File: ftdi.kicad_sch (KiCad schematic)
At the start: 24 parts, among them U1 FT2232H-56Q, U11 93LC56CT-IMC, Y4 ABM8G-12M-18-D2Y-T

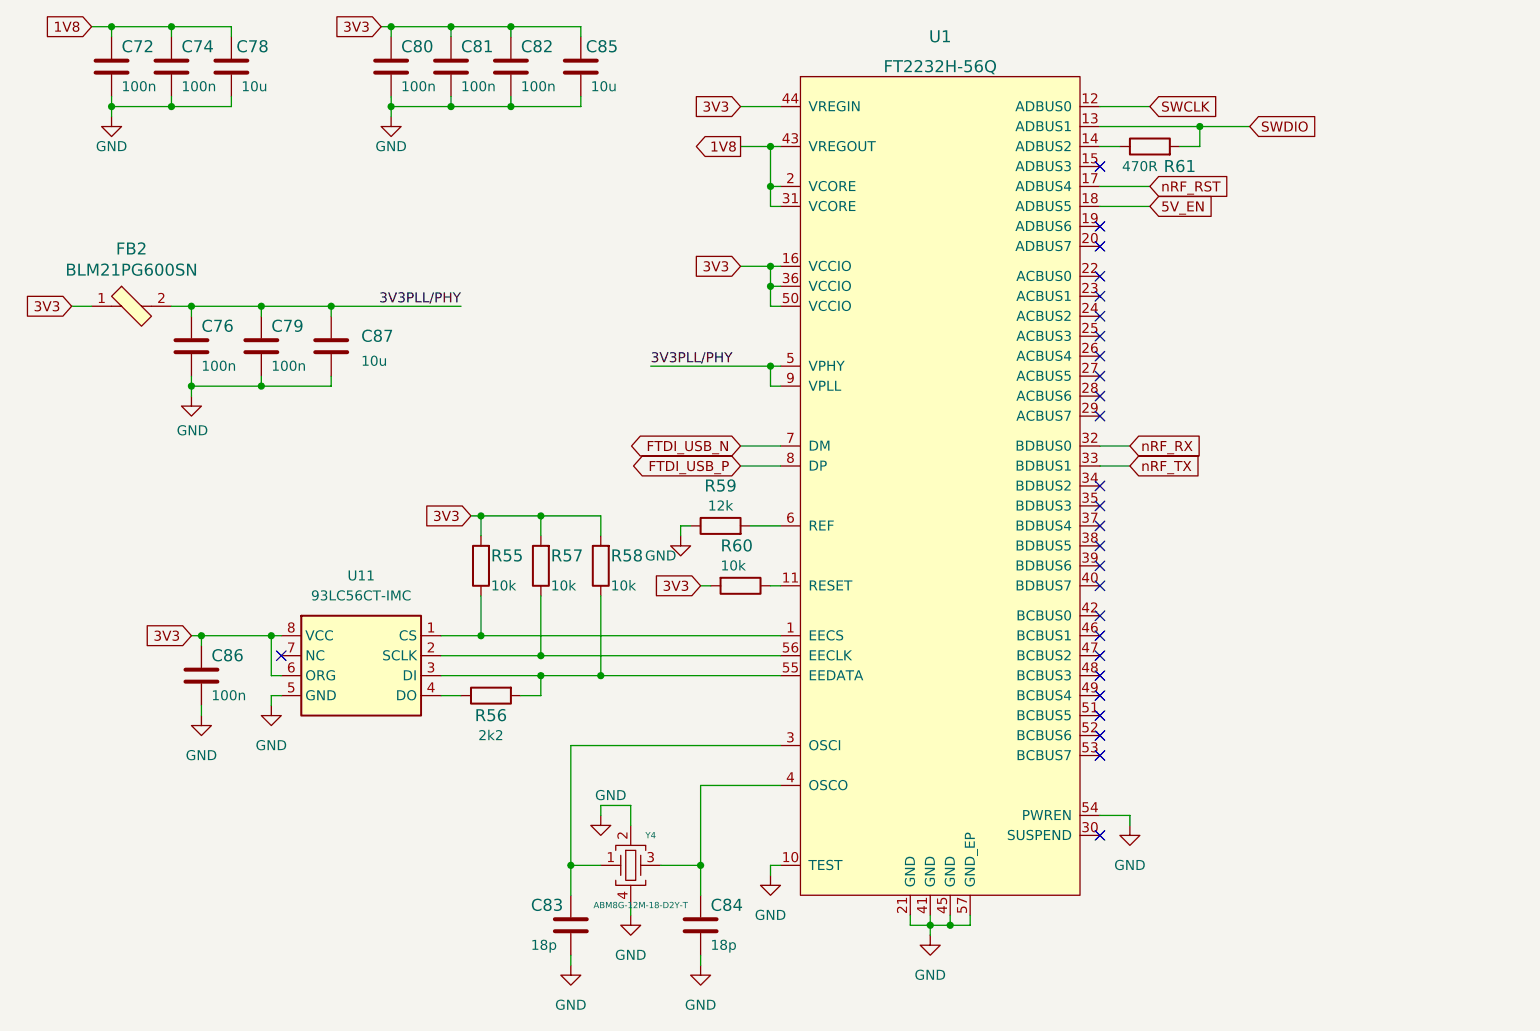
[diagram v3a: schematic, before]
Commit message: Replaced ft2232 with ft4232H
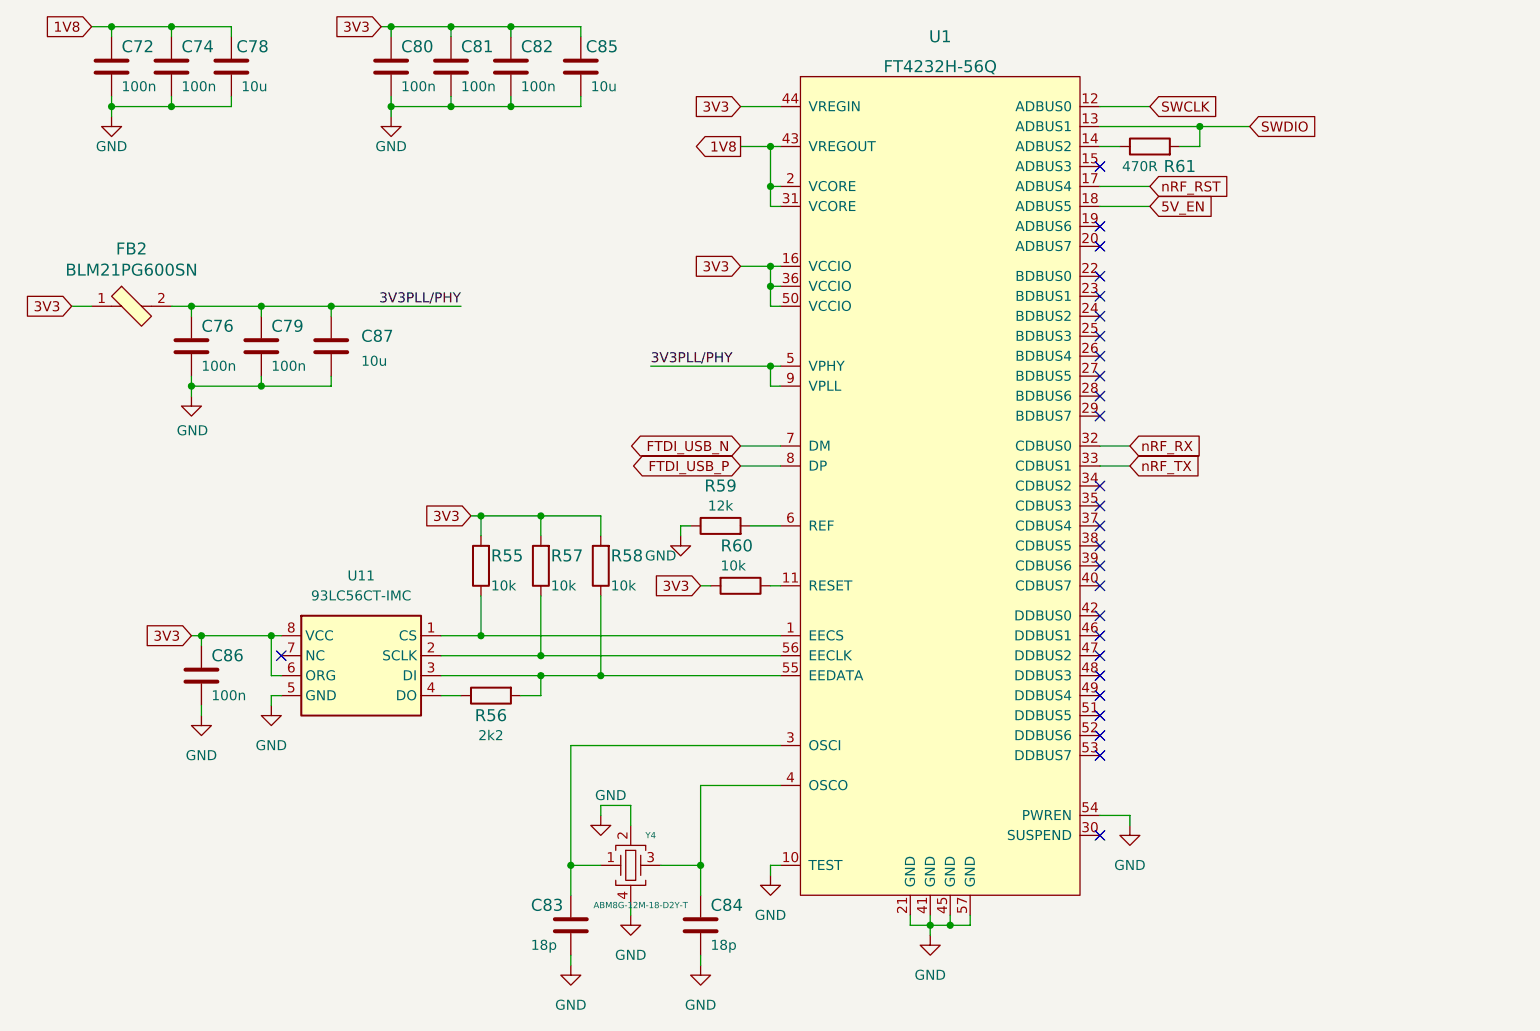
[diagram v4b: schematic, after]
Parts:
- U1: value FT2232H-56Q -> FT4232H-56Q; symbol antmicroInterfaceControllers:FT2232H-56Q -> antmicroInterfaceControllers:FT4232H-56Q; MPN FT2232HQ-TRAY -> FT4232H-56Q-REEL
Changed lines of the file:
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@@
     (pin "1")
   )
-  (symbol (lib_id "antmicroInterfaceControllers:FT2232H-56Q") (at 143.51 96.52 0) (unit 1)
+  (symbol (lib_id "antmicroInterfaceControllers:FT4232H-56Q") (at 143.51 96.52 0) (unit 1)
     (in_bom yes) (on_board yes) (fields_autoplaced)
     (property "Reference" "U1" (id 0) (at 143.51 33.02 0)
       (effects (font (size 1.524 1.524)))
     )
-    (property "Value" "FT2232H-56Q" (id 1) (at 143.51 36.83 0)
+    (property "Value" "FT4232H-56Q" (id 1) (at 143.51 36.83 0)
       (effects (font (size 1.524 1.524)))
     )
@@
       (effects (font (size 1.524 1.524)) (justify left) hide)
     )
-    (property "Datasheet" "https://www.ftdichip.com/Support/Documents/DataSheets/ICs/DS_FT2232H.pdf" (id 3) (at 148.59 86.36 0)
+    (property "Datasheet" "https://www.ftdichip.com/Support/Documents/DataSheets/ICs/DS_FT4232H.pdf" (id 3) (at 148.59 86.36 0)
       (effects (font (size 1.524 1.524)) (justify left) hide)
     )
@@
       (effects (font (size 1.524 1.524)) (justify left) hide)
     )
-    (property "MPN" "FT2232HQ-TRAY" (id 5) (at 148.59 82.55 0)
+    (property "MPN" "FT4232H-56Q-REEL" (id 5) (at 148.59 82.55 0)
       (effects (font (size 1.524 1.524)) (justify left) hide)
     )

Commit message: Loclib
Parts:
- C72, C74, C76, C79, C80, C81, C82, C86: footprint antmicro-footprints:0402-cap -> m2-smart-iot-module-footprints:0402-cap; symbol antmicroCapacitors0402:C_100n_0402 -> m2-smart-iot-module:C_100n_0402
- C83, C84: footprint antmicro-footprints:0402-cap -> m2-smart-iot-module-footprints:0402-cap; symbol antmicroCapacitors0402:C_18p_0402 -> m2-smart-iot-module:C_18p_0402
- C87: footprint antmicro-footprints:0603-cap -> m2-smart-iot-module-footprints:0603-cap; symbol antmicroCapacitors0603:C_10u_0603 -> m2-smart-iot-module:C_10u_0603
- R55, R57, R58, R60: footprint antmicro-footprints:0402-res -> m2-smart-iot-module-footprints:0402-res; symbol antmicroResistors0402:R_10k_0402 -> m2-smart-iot-module:R_10k_0402
- R56: footprint antmicro-footprints:0402-res -> m2-smart-iot-module-footprints:0402-res; symbol antmicroResistors0402:R_2k2_0402 -> m2-smart-iot-module:R_2k2_0402
- R59: footprint antmicro-footprints:0402-res -> m2-smart-iot-module-footprints:0402-res; symbol antmicroResistors0402:R_12k_0402 -> m2-smart-iot-module:R_12k_0402
- R61: footprint antmicro-footprints:0402-res -> m2-smart-iot-module-footprints:0402-res; symbol antmicroResistors0402:R_470R_0402 -> m2-smart-iot-module:R_470R_0402
- U1: footprint antmicro-footprints:QFN-56-1EP_8x8mm_P0.5mm_EP5.5.9x5.9mm -> m2-smart-iot-module-footprints:QFN-56-1EP_8x8mm_P0.5mm_EP5.5.9x5.9mm; symbol antmicroInterfaceControllers:FT4232H-56Q -> m2-smart-iot-module:FT4232H-56Q
- U11: footprint antmicro-footprints:DFN-8_2x3mm -> m2-smart-iot-module-footprints:DFN-8_2x3mm; symbol antmicroMemory:93LC56CT-IMC -> m2-smart-iot-module:93LC56CT-IMC
- Y4: footprint antmicro-footprints:KX-7 -> m2-smart-iot-module-footprints:KX-7; symbol antmicroCrystals:ABM8G-12.000MHZ-18-D2Y-T -> m2-smart-iot-module:ABM8G-12.000MHZ-18-D2Y-T

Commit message: Rev bump to 1.2.8
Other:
- title: (none) -> M.2 Smart IoT Module

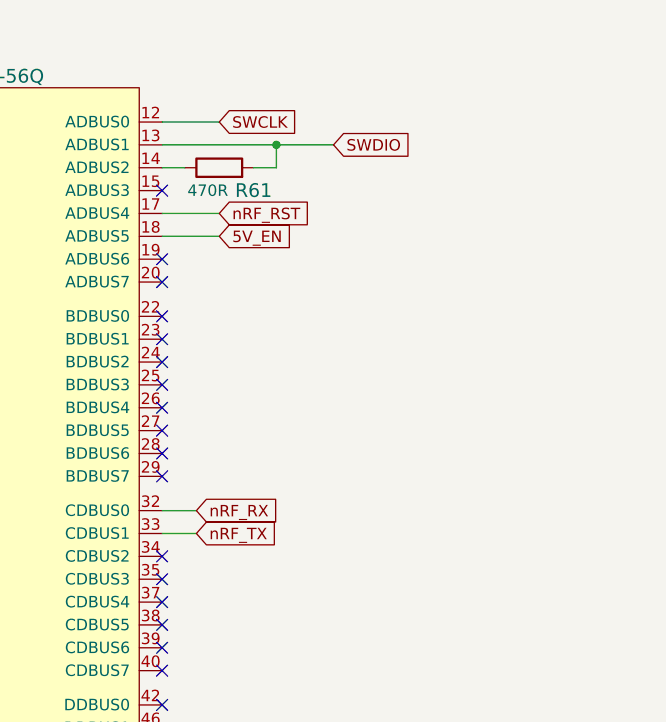
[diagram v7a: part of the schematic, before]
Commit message: Add OR resistors to outputs of the PCIE-USB bridge and FTDI
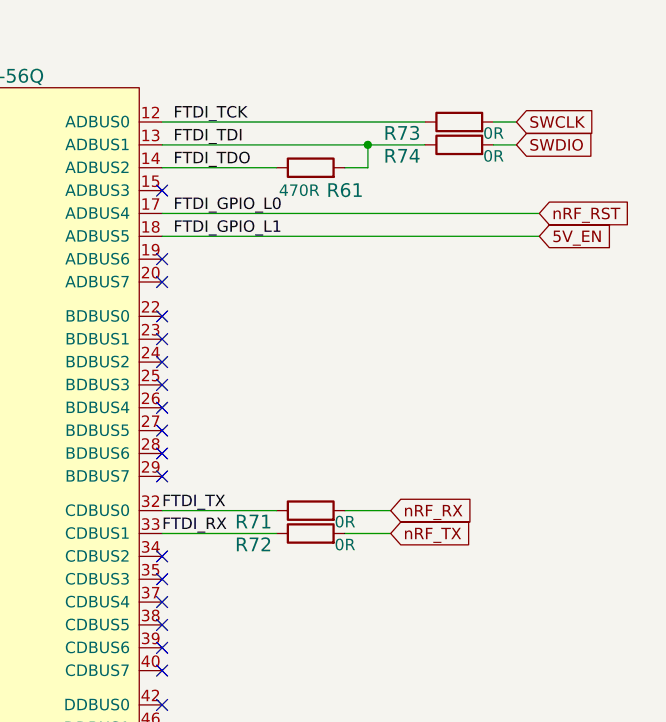
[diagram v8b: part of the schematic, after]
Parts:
- added R71, R72, R73, R74: R_0R_0402, m2-smart-iot-module-footprints:0402-res, symbol m2-smart-iot-module:R_0R_0402
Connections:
- net SWCLK: now also R73.2; no longer U1.12 (ADBUS0)
- net SWDIO: now also R74.2; no longer R61.2, U1.13 (ADBUS1)
- net nRF_RX: now also R71.2; no longer U1.32 (CDBUS0)
- net nRF_TX: now also R72.2; no longer U1.33 (CDBUS1)
- net FTDI_TDO: now reaches R61.1, U1.14 (ADBUS2)
- new net FTDI_RX: R72.1, U1.33 (CDBUS1)
- new net FTDI_TCK: R73.1, U1.12 (ADBUS0)
- new net FTDI_TDI: R61.2, R74.1, U1.13 (ADBUS1)
- new net FTDI_TX: R71.1, U1.32 (CDBUS0)
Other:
- moved on the sheet: R61
